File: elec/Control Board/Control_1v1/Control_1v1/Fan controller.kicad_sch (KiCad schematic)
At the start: 37 parts, among them J10 Conn_01x05, J11 Conn_01x04, J12 Conn_01x07, J20 Conn_01x04, J6 DB25_Female_MountingHoles, J9 Conn_01x04, Q2 NCE01P30K, Q601 BSS138

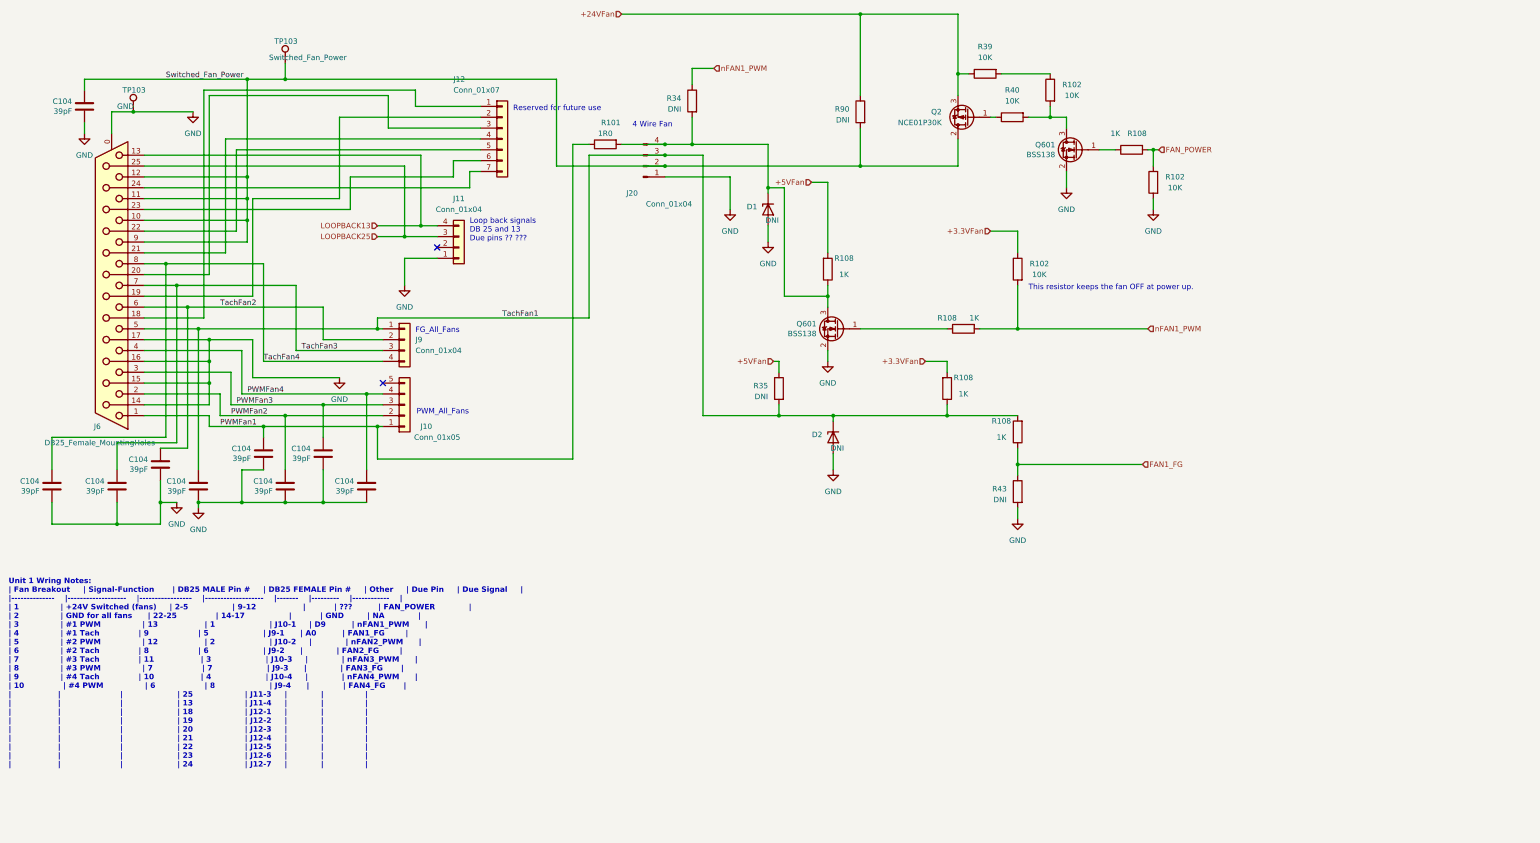
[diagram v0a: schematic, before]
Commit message: Add sheet with title block.
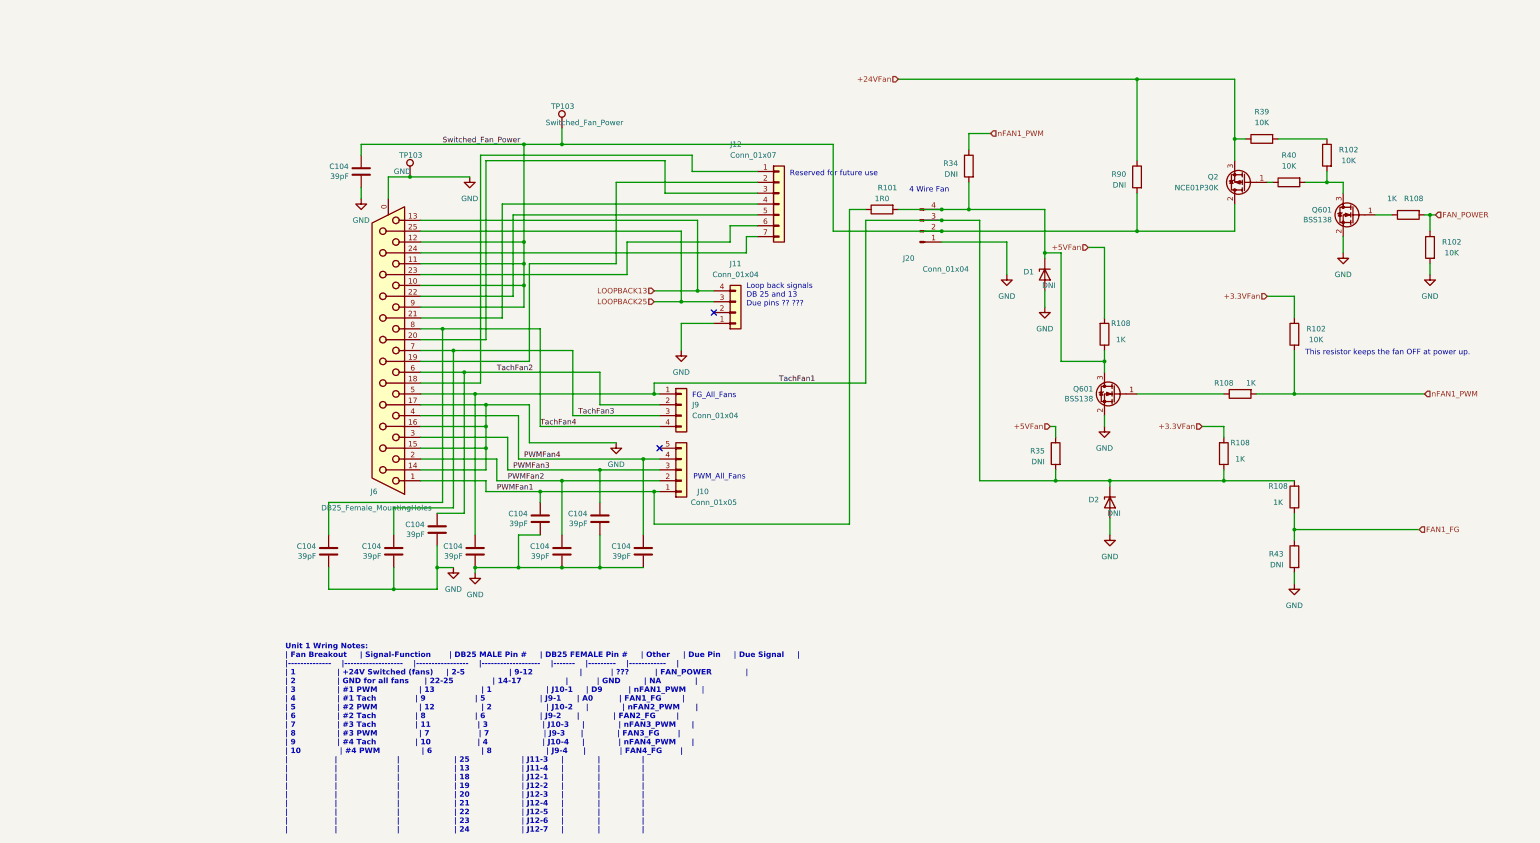
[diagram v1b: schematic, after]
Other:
- company: (none) -> Public Invention
- title: (none) -> Control Interconnect Board
- moved on the sheet: C104, D1, D2, J10, J11, J12, J20, J6, J9, Q2, Q601, R101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

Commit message: Fix J10 backwards.
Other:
- title: Control Interconnect Board -> Control Interconnect Board OEDCS
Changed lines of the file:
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@@
   (paper "USLedger")
   (title_block
-    (title "Control Interconnect Board")
+    (title "Control Interconnect Board OEDCS")
     (date "2023-10-10")
     (rev "Rev 1.1")
     (company "Public Invention")
-    (comment 1 "Contributor: Lawrence Kinceloe")
+    (comment 1 "GNU Affero General Public License v3.0")
+    (comment 2 "Contributor: Lawrence Kinceloe")
+    (comment 3 "Drawn By: (Forrest) Lee Erickson")
   )
   (junction (at 308.61 151.13) (diameter 0) (color 0 0 0 0)

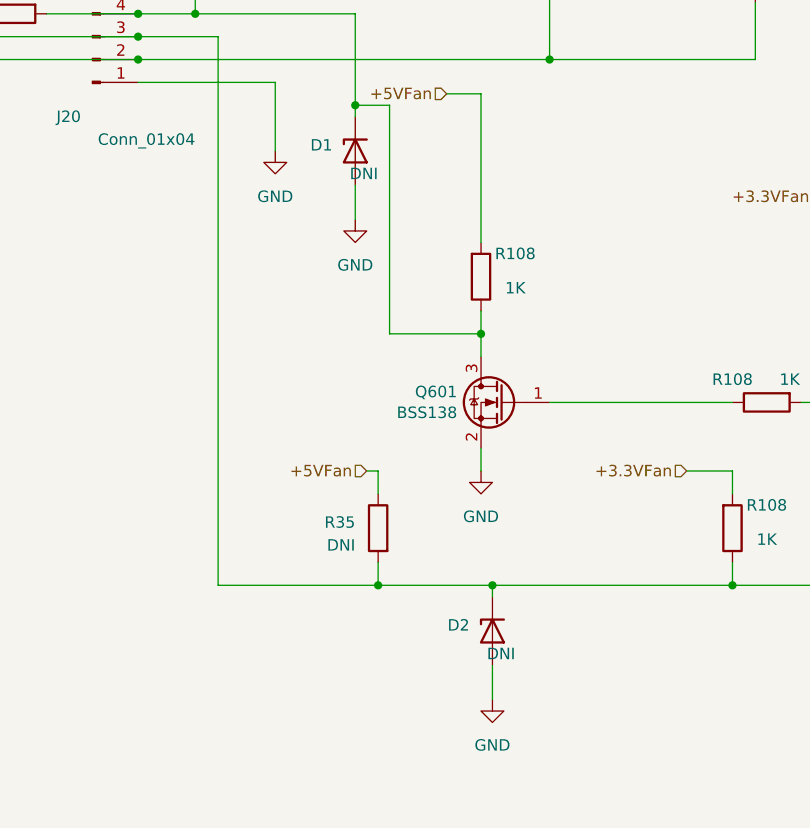
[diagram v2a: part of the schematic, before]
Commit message: Route AUX power sensors.
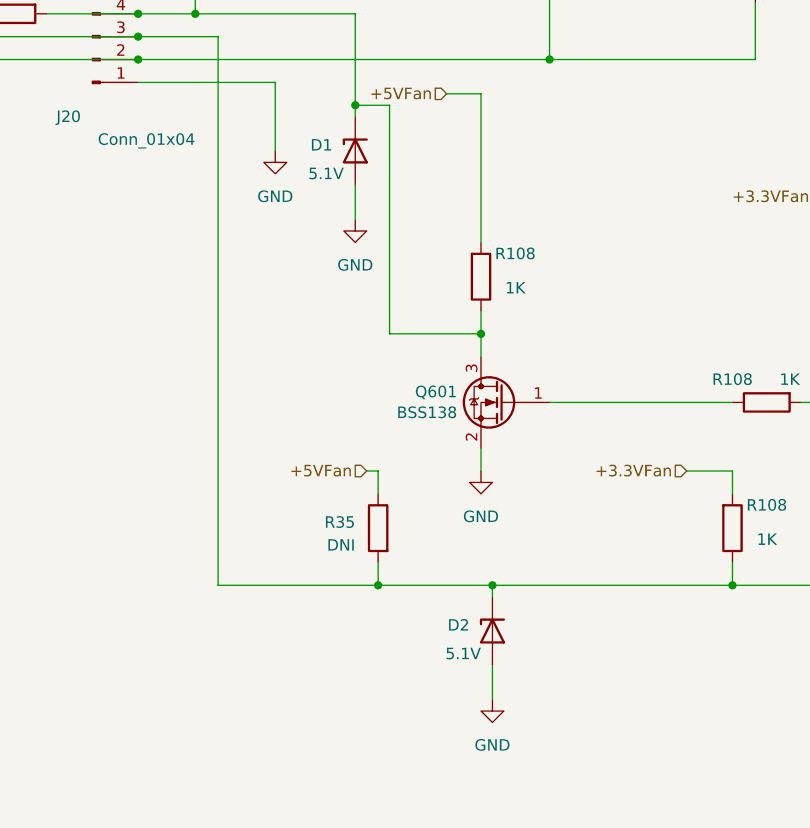
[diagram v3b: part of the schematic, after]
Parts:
- D1, D2: value DNI -> 5.1V; Cost 1000000 -> 0.0433; Distributor 1 (none) -> JLCPCB; Distributor 1 PN (none) -> C841097; MPN (none) -> DL4733A; Manufacturer (none) -> LGE
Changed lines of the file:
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@@
       (effects (font (size 1.27 1.27)) (justify left))
     )
-    (property "Value" "DNI " (at 252.73 93.98 90)
+    (property "Value" "5.1V" (at 248.92 93.98 90)
       (effects (font (size 1.27 1.27)) (justify left))
     )
@@
       (effects (font (size 1.27 1.27)) hide)
     )
-    (property "Cost" "1000000" (at 250.19 91.44 0)
+    (property "Cost" "0.0433" (at 250.19 91.44 0)
+      (effects (font (size 1.27 1.27)) hide)
+    )
+    (property "Description" "±5% Single 1W 5.1V MELF Zener Diodes ROHS" (at 250.19 91.44 0)
+      (effects (font (size 1.27 1.27)) hide)
+    )
+    (property "Distributor 1" "JLCPCB" (at 250.19 91.44 0)
+      (effects (font (size 1.27 1.27)) hide)
+    )
+    (property "Distributor 1 PN" "C841097" (at 250.19 91.44 0)
+      (effects (font (size 1.27 1.27)) hide)
+    )
+    (property "MPN" "DL4733A" (at 250.19 91.44 0)
+      (effects (font (size 1.27 1.27)) hide)
+    )
+    (property "Manufacturer" "LGE" (at 250.19 91.44 0)
       (effects (font (size 1.27 1.27)) hide)
     )
@@
       (effects (font (size 1.27 1.27)) (justify left))
     )
-    (property "Value" "DNI " (at 267.97 147.32 90)
+    (property "Value" "5.1V" (at 264.16 147.32 90)
       (effects (font (size 1.27 1.27)) (justify left))
     )
@@
       (effects (font (size 1.27 1.27)) hide)
     )
-    (property "Cost" "1000000" (at 265.43 144.78 0)
+    (property "Cost" "0.0433" (at 265.43 144.78 0)
       (effects (font (size 1.27 1.27)) hide)
     )
+    (property "Description" "±5% Single 1W 5.1V MELF Zener Diodes ROHS" (at 265.43 144.78 0)
+      (effects (font (size 1.27 1.27)) hide)
+    )
+    (property "Distributor 1" "JLCPCB" (at 265.43 144.78 0)
+      (effects (font (size 1.27 1.27)) hide)
+    )
+    (property "Distributor 1 PN" "C841097" (at 265.43 144.78 0)
+      (effects (font (size 1.27 1.27)) hide)
+    )
+    (property "MPN" "DL4733A" (at 265.43 144.78 0)
+      (effects (font (size 1.27 1.27)) hide)
+    )
+    (property "Manufacturer" "LGE" (at 265.43 144.78 0)
+      (effects (font (size 1.27 1.27)) hide)
+    )

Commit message: Add power shutdown button. Add thermocouple ground screw terminals. Isolate SCL from SDA traces. Make first cut BOM.
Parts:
- R101: LongLead (none) -> NO
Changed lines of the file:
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@@
+      (effects (font (size 1.27 1.27)) hide)
+    )
+    (property "LongLead" "NO" (at 212.09 76.2 0)
       (effects (font (size 1.27 1.27)) hide)
     )
